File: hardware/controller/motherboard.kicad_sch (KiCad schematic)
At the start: 49 parts, among them J10 TC2030, J2 Molex PicoBlade, J3 Conn_02x06_Odd_Even, J4 AFB10-S18LCA-00, J5 726386-2, J6 Conn_Coaxial_Small, J7 AFB10-S06LCA-00, J9 AFC11-S12ICA-00, Q1 PMZB350UPE,315, SW90 SW_Push, U1 NRF52840, U2 nPM1300-QEAA, Y1 32MHz, Y2 32.768 kHz

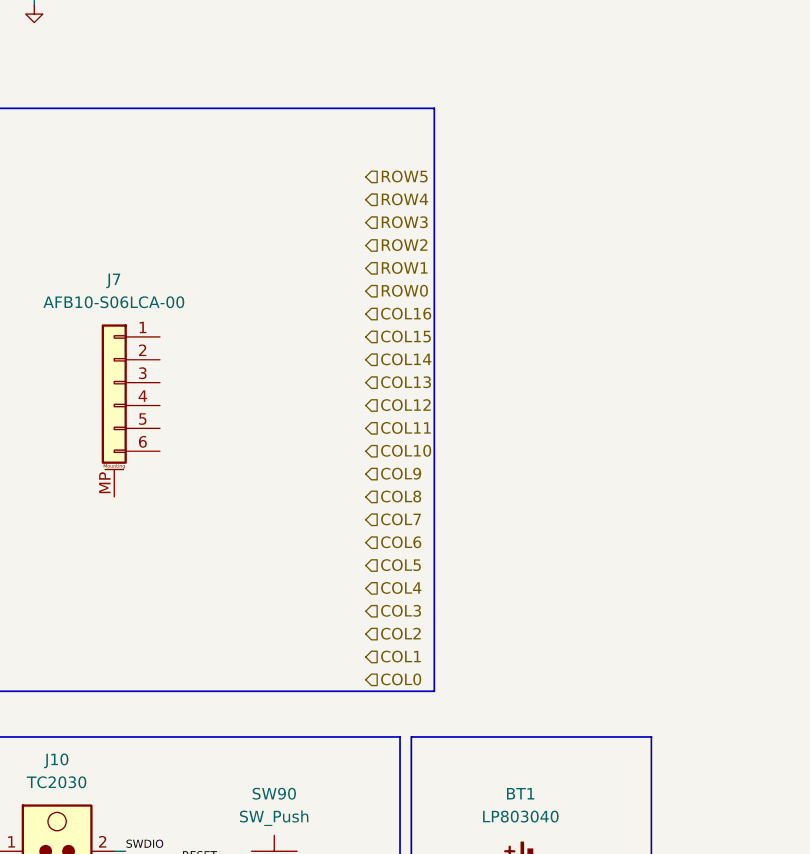
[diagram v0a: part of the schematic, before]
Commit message: refactor(controller): remove matrix sheet (moved to membrane)
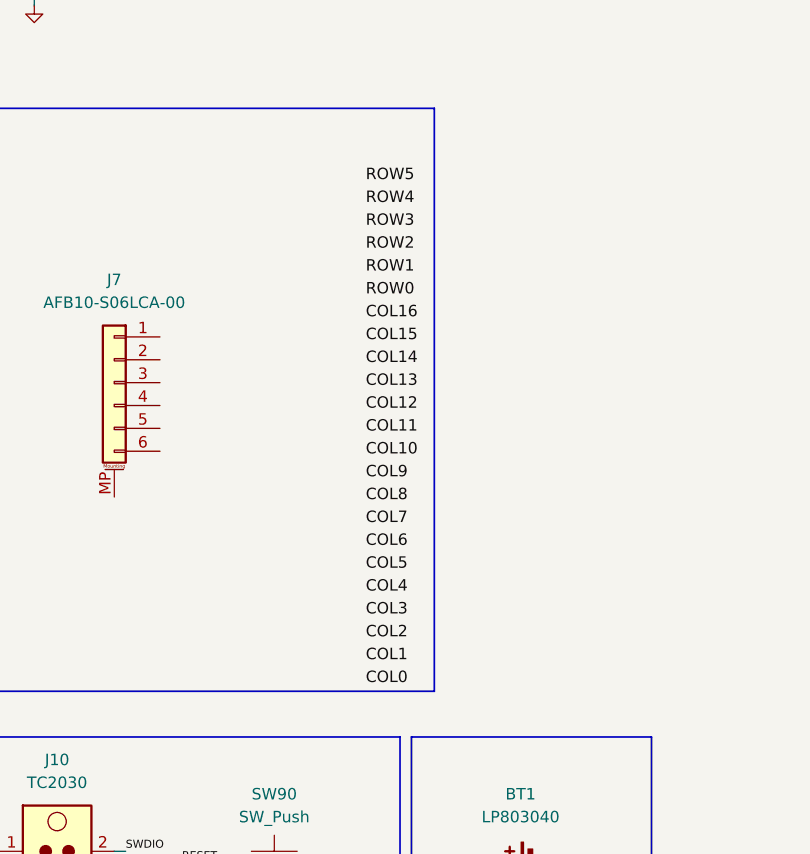
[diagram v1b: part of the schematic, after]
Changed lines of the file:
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@@
 		)
 	)
-	(hierarchical_label "COL6"
-		(shape input)
+	(label "COL6"
 		(at 140.97 205.74 0)
 		(effects
@@
 		)
 	)
-	(hierarchical_label "COL10"
-		(shape input)
+	(label "COL10"
 		(at 140.97 195.58 0)
 		(effects
@@
 		)
 	)
-	(hierarchical_label "COL7"
-		(shape input)
+	(label "COL7"
 		(at 140.97 203.2 0)
 		(effects
@@
 		)
 	)
-	(hierarchical_label "COL11"
-		(shape input)
+	(label "COL11"
 		(at 140.97 193.04 0)
 		(effects
@@
 		)
 	)
-	(hierarchical_label "COL15"
-		(shape input)
+	(label "COL15"
 		(at 140.97 182.88 0)
 		(effects
@@
 		)
 	)
-	(hierarchical_label "COL3"
-		(shape input)
+	(label "COL3"
 		(at 140.97 213.36 0)
 		(effects
@@
 		)
 	)
-	(hierarchical_label "ROW5"
-		(shape input)
+	(label "ROW5"
 		(at 140.97 165.1 0)
 		(effects
@@
 		)
 	)
-	(hierarchical_label "COL2"
-		(shape input)
+	(label "COL2"
 		(at 140.97 215.9 0)
 		(effects
@@
 		)
 	)
-	(hierarchical_label "ROW4"
-		(shape input)
+	(label "ROW4"
 		(at 140.97 167.64 0)
 		(effects
@@
 		)
 	)
-	(hierarchical_label "COL16"
-		(shape input)
+	(label "COL16"
 		(at 140.97 180.34 0)
 		(effects
@@
 		)
 	)
-	(hierarchical_label "COL13"
-		(shape input)
+	(label "COL13"
 		(at 140.97 187.96 0)
 		(effects
@@
 		)
 	)
-	(hierarchical_label "COL9"
-		(shape input)
+	(label "COL9"
 		(at 140.97 198.12 0)
 		(effects
@@
 		)
 	)
-	(hierarchical_label "ROW2"
-		(shape input)
+	(label "ROW2"
 		(at 140.97 172.72 0)
 		(effects
@@
 		)
 	)
-	(hierarchical_label "COL4"
-		(shape input)
+	(label "COL4"
 		(at 140.97 210.82 0)
 		(effects
@@
 		)
 	)
-	(hierarchical_label "ROW3"
-		(shape input)
+	(label "ROW3"
 		(at 140.97 170.18 0)
 		(effects
@@
 		)
 	)
-	(hierarchical_label "COL14"
-		(shape input)
+	(label "COL14"
 		(at 140.97 185.42 0)
 		(effects
@@
 		)
 	)
-	(hierarchical_label "COL1"
-		(shape input)
+	(label "COL1"
 		(at 140.97 218.44 0)
 		(effects
@@
 		)
 	)
-	(hierarchical_label "COL5"
-		(shape input)
+	(label "COL5"
 		(at 140.97 208.28 0)
 		(effects
@@
 		)
 	)
-	(hierarchical_label "ROW1"
-		(shape input)
+	(label "ROW1"
 		(at 140.97 175.26 0)
 		(effects
@@
 		)
 	)
-	(hierarchical_label "COL8"
-		(shape input)
+	(label "COL8"
 		(at 140.97 200.66 0)
 		(effects
@@
 		)
 	)
-	(hierarchical_label "ROW0"
-		(shape input)
+	(label "ROW0"
 		(at 140.97 177.8 0)
 		(effects
@@
 		)
 	)
-	(hierarchical_label "COL0"
-		(shape input)
+	(label "COL0"
 		(at 140.97 220.98 0)
 		(effects
@@
 		)
 	)
-	(hierarchical_label "COL12"
-		(shape input)
+	(label "COL12"
 		(at 140.97 190.5 0)
 		(effects
